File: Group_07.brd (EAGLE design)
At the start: 62.2 x 74.9 mm, 29 parts, among them J1 POWER_JACKPTH_LOCK, U1 +12v, U3 TCA9546ASO16, U4 TMUX1208

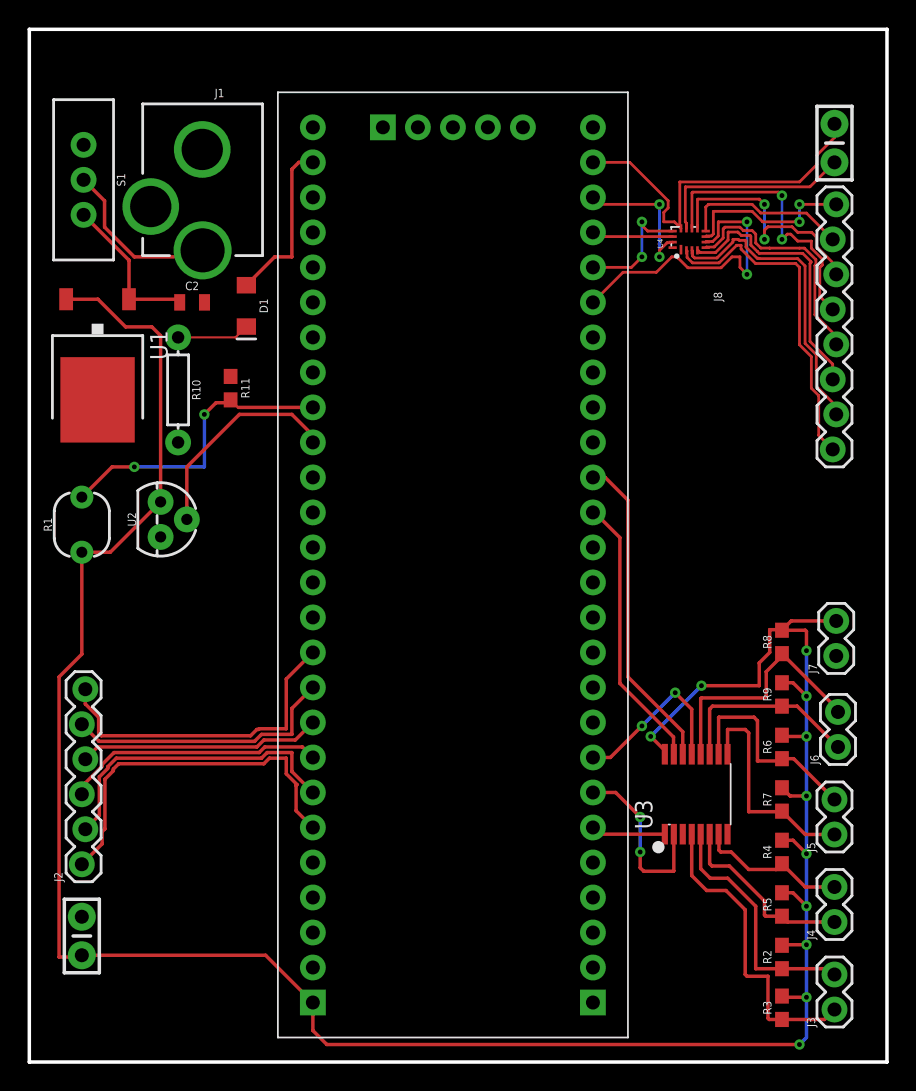
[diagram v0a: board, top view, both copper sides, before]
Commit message: controllo ratsnest
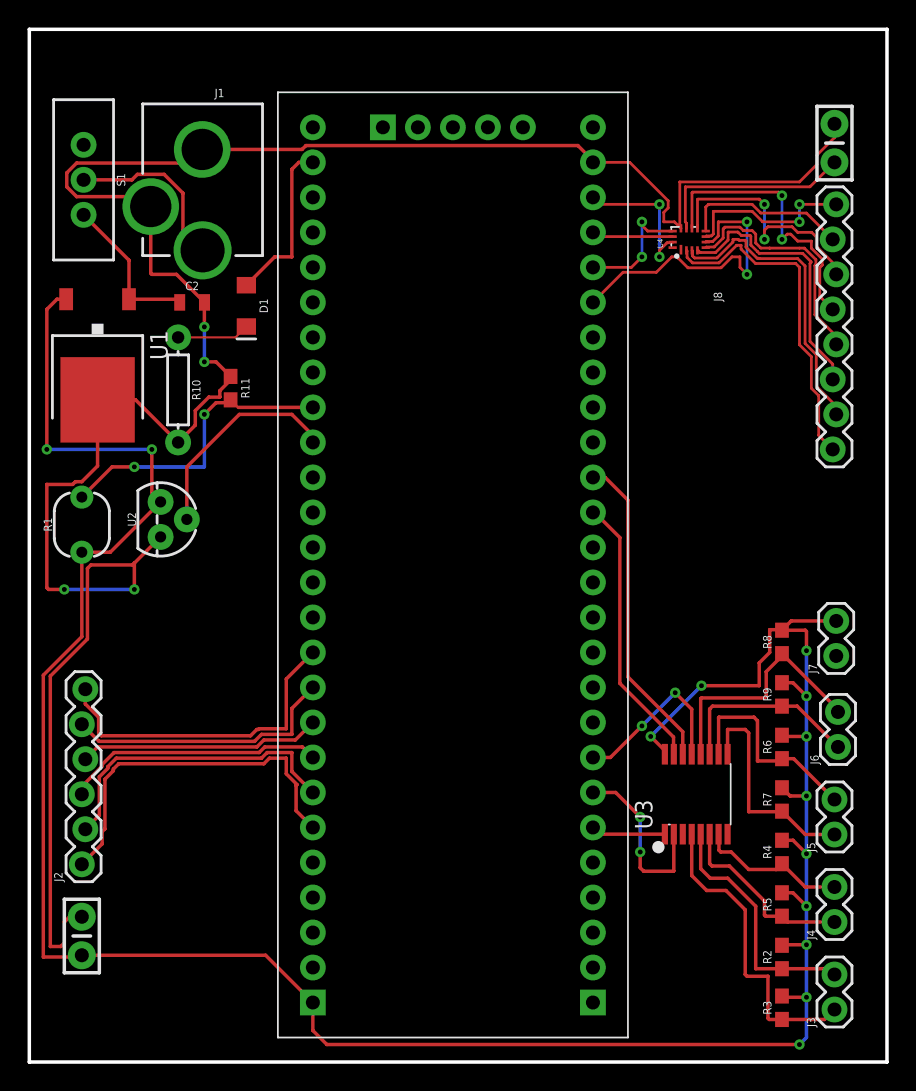
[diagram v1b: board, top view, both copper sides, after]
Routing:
- net GND: track 27.1 -> 168.3 mm, vias 0 -> 4
- net 5V: track 196.1 -> 201.3 mm, vias 11 -> 13
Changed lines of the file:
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@@
 <wire x1="56.642" y1="63.5" x2="58.42" y2="65.278" width="0.2032" layer="1"/>
 <wire x1="47.598" y1="63.5" x2="56.642" y2="63.5" width="0.2032" layer="1"/>
-<wire x1="2.673" y1="55.346" x2="4.979" y2="55.346" width="0.254" layer="1"/>
-<wire x1="6.985" y1="53.34" x2="8.89" y2="53.34" width="0.254" layer="1"/>
-<wire x1="8.89" y1="53.34" x2="9.525" y2="52.705" width="0.254" layer="1"/>
-<wire x1="9.525" y1="52.705" x2="9.525" y2="40.64" width="0.254" layer="1"/>
-<wire x1="4.979" y1="55.346" x2="6.985" y2="53.34" width="0.254" layer="1"/>
 <wire x1="9.525" y1="40.64" x2="5.874" y2="36.989" width="0.254" layer="1"/>
 <wire x1="5.874" y1="36.989" x2="3.81" y2="36.989" width="0.254" layer="1"/>
-<wire x1="3.81" y1="36.989" x2="3.81" y2="29.591" width="0.254" layer="1"/>
-<wire x1="3.81" y1="29.591" x2="2.159" y2="27.94" width="0.254" layer="1"/>
-<wire x1="2.159" y1="27.94" x2="2.159" y2="7.62" width="0.254" layer="1"/>
-<wire x1="2.159" y1="7.62" x2="3.683" y2="7.62" width="0.254" layer="1"/>
+<wire x1="3.81" y1="36.989" x2="3.81" y2="30.861" width="0.254" layer="1"/>
+<wire x1="3.81" y1="30.861" x2="1.016" y2="28.067" width="0.254" layer="1"/>
+<wire x1="1.016" y1="28.067" x2="1.016" y2="7.62" width="0.254" layer="1"/>
+<wire x1="1.016" y1="7.62" x2="3.683" y2="7.62" width="0.254" layer="1"/>
 <wire x1="3.683" y1="7.62" x2="3.81" y2="7.747" width="0.1524" layer="1"/>
 <wire x1="3.81" y1="7.747" x2="17.145" y2="7.747" width="0.254" layer="1"/>
@@
 <wire x1="20.574" y1="2.286" x2="20.574" y2="4.318" width="0.254" layer="1"/>
 <wire x1="55.88" y1="1.27" x2="21.59" y2="1.27" width="0.254" layer="1"/>
+<wire x1="9.525" y1="40.64" x2="8.89" y2="41.275" width="0.254" layer="1"/>
+<wire x1="8.89" y1="41.275" x2="8.89" y2="44.45" width="0.254" layer="1"/>
+<via x="8.89" y="44.45" extent="1-16" drill="0.35"/>
+<wire x1="8.89" y1="44.45" x2="1.27" y2="44.45" width="0.254" layer="16"/>
+<via x="1.27" y="44.45" extent="1-16" drill="0.35"/>
+<wire x1="1.27" y1="44.45" x2="1.27" y2="54.61" width="0.254" layer="1"/>
+<wire x1="1.27" y1="54.61" x2="2.006" y2="55.346" width="0.254" layer="1"/>
+<wire x1="2.006" y1="55.346" x2="2.673" y2="55.346" width="0.254" layer="1"/>
+<wire x1="54.61" y1="31.33" x2="47.679" y2="60.49" width="0" layer="19" extent="1-1"/>
 </signal>
 <signal name="N$1">
 <contactref element="J1" pad="PWR"/>
 <contactref element="S1" pad="2"/>
-<wire x1="3.937" y1="64.008" x2="5.461" y2="62.484" width="0.254" layer="1"/>
-<wire x1="7.62" y1="58.42" x2="12.0998" y2="58.42" width="0.254" layer="1"/>
-<wire x1="12.0998" y1="58.42" x2="12.573" y2="58.8932" width="0.254" layer="1"/>
-<wire x1="5.461" y1="62.484" x2="5.461" y2="60.579" width="0.254" layer="1"/>
-<wire x1="5.461" y1="60.579" x2="7.62" y2="58.42" width="0.254" layer="1"/>
+<wire x1="3.937" y1="64.008" x2="7.4436625" y2="64.008" width="0.254" layer="1"/>
+<wire x1="7.4436625" y1="64.008" x2="7.8434625" y2="64.4078" width="0.254" layer="1"/>
+<wire x1="7.8434625" y1="64.4078" x2="9.7793375" y2="64.4078" width="0.254" layer="1"/>
+<wire x1="9.7793375" y1="64.4078" x2="11.1482" y2="63.0389375" width="0.254" layer="1"/>
+<wire x1="11.1482" y1="60.318" x2="12.573" y2="58.8932" width="0.254" layer="1"/>
+<wire x1="11.1482" y1="63.0389375" x2="11.1482" y2="60.318" width="0.254" layer="1"/>
 </signal>
 <signal name="GND">
@@
 <wire x1="46.0344" y1="61.65033125" x2="46.3522" y2="61.96813125" width="0.2032" layer="1"/>
 <wire x1="46.3522" y1="62.49186875" x2="43.56606875" y2="65.278" width="0.2032" layer="1"/>
-<wire x1="43.56606875" y1="65.278" x2="40.894" y2="65.278" width="0.2032" layer="1"/>
+<wire x1="43.56606875" y1="65.278" x2="41.021" y2="65.278" width="0.2032" layer="1"/>
+<wire x1="41.021" y1="65.278" x2="40.894" y2="65.278" width="0.2032" layer="1"/>
 <wire x1="46.0344" y1="60.96" x2="46.809" y2="60.96" width="0.2032" layer="1"/>
 <wire x1="46.809" y1="60.96" x2="47.279" y2="60.49" width="0.2032" layer="1"/>
@@
 <wire x1="55.88" y1="63.8556" x2="57.15" y2="65.1256" width="0.2032" layer="1"/>
 <wire x1="57.15" y1="65.1256" x2="57.15" y2="65.80405625" width="0.2032" layer="1"/>
-<wire x1="58.42" y1="67.07405625" x2="58.42" y2="68.072" width="0.2032" layer="1"/>
-<wire x1="57.15" y1="65.80405625" x2="58.42" y2="67.07405625" width="0.2032" layer="1"/>
-<wire x1="50.662" y1="16.531" x2="47.412" y2="16.531" width="0" layer="19" extent="1-1"/>
-<wire x1="58.547" y1="29.464" x2="50.662" y2="16.531" width="0" layer="19" extent="1-1"/>
-<wire x1="9.525" y1="38.1" x2="10.795" y2="44.958" width="0" layer="19" extent="1-1"/>
-<wire x1="3.81" y1="10.541" x2="9.525" y2="38.1" width="0" layer="19" extent="1-1"/>
+<wire x1="58.42" y1="67.07405625" x2="57.15" y2="65.80405625" width="0.2032" layer="1"/>
+<wire x1="10.795" y1="44.958" x2="12.0424" y2="46.2054" width="0.254" layer="1"/>
+<wire x1="13.807" y1="48.2414" x2="13.8256" y2="48.26" width="0.254" layer="1"/>
+<wire x1="12.0424" y1="46.2054" x2="12.0424" y2="47.2623875" width="0.254" layer="1"/>
+<wire x1="12.0424" y1="47.2623875" x2="13.0214125" y2="48.2414" width="0.254" layer="1"/>
+<wire x1="13.0214125" y1="48.2414" x2="13.807" y2="48.2414" width="0.254" layer="1"/>
+<wire x1="13.8256" y1="48.26" x2="13.8256" y2="48.71073125" width="0.254" layer="1"/>
+<wire x1="14.605" y1="49.49013125" x2="14.605" y2="49.745" width="0.254" layer="1"/>
+<wire x1="13.8256" y1="48.71073125" x2="14.605" y2="49.49013125" width="0.254" layer="1"/>
+<wire x1="14.605" y1="49.745" x2="13.55" y2="50.8" width="0.254" layer="1"/>
+<wire x1="13.55" y1="50.8" x2="12.7" y2="50.8" width="0.254" layer="1"/>
+<via x="12.7" y="50.8" extent="1-16" drill="0.35"/>
+<wire x1="12.7" y1="50.8" x2="12.7" y2="53.34" width="0.254" layer="16"/>
+<via x="12.7" y="53.34" extent="1-16" drill="0.35"/>
+<wire x1="12.7" y1="53.34" x2="12.7" y2="55.107" width="0.254" layer="1"/>
+<wire x1="12.7" y1="55.107" x2="12.711" y2="55.118" width="0.254" layer="1"/>
+<wire x1="12.711" y1="55.118" x2="10.679" y2="57.15" width="0.254" layer="1"/>
+<wire x1="10.679" y1="57.15" x2="8.89" y2="57.15" width="0.254" layer="1"/>
+<wire x1="8.89" y1="57.15" x2="8.8114" y2="57.2286" width="0.254" layer="1"/>
+<wire x1="8.8114" y1="57.2286" x2="8.8114" y2="62.071" width="0.254" layer="1"/>
+<wire x1="3.4319875" y1="62.7888" x2="2.7178" y2="63.5029875" width="0.254" layer="1"/>
+<wire x1="2.7178" y1="63.5029875" x2="2.7178" y2="64.5130125" width="0.254" layer="1"/>
+<wire x1="2.7178" y1="64.5130125" x2="3.4319875" y2="65.2272" width="0.254" layer="1"/>
+<wire x1="8.8114" y1="62.071" x2="8.0936" y2="62.7888" width="0.254" layer="1"/>
+<wire x1="8.0936" y1="62.7888" x2="3.4319875" y2="62.7888" width="0.254" layer="1"/>
+<wire x1="11.5608" y1="65.2272" x2="12.5476" y2="66.214" width="0.254" layer="1"/>
+<wire x1="3.4319875" y1="65.2272" x2="11.5608" y2="65.2272" width="0.254" layer="1"/>
+<wire x1="12.5476" y1="66.214" x2="19.78833125" y2="66.214" width="0.254" layer="1"/>
+<wire x1="19.78833125" y1="66.214" x2="20.06973125" y2="66.4954" width="0.254" layer="1"/>
+<wire x1="20.06973125" y1="66.4954" x2="39.8036" y2="66.4954" width="0.254" layer="1"/>
+<wire x1="39.8036" y1="66.4954" x2="41.021" y2="65.278" width="0.254" layer="1"/>
+<wire x1="9.525" y1="38.1" x2="7.62" y2="36.195" width="0.254" layer="1"/>
+<wire x1="7.62" y1="36.195" x2="7.493" y2="36.068" width="0.254" layer="1"/>
+<wire x1="7.493" y1="36.068" x2="4.46953125" y2="36.068" width="0.254" layer="1"/>
+<wire x1="4.2164" y1="35.81486875" x2="4.2164" y2="30.6926625" width="0.254" layer="1"/>
+<wire x1="1.524" y1="28.0002625" x2="1.524" y2="8.382" width="0.254" layer="1"/>
+<wire x1="4.2164" y1="30.6926625" x2="1.524" y2="28.0002625" width="0.254" layer="1"/>
+<wire x1="1.524" y1="8.382" x2="2.286" y2="8.382" width="0.254" layer="1"/>
+<wire x1="2.286" y1="8.382" x2="2.54" y2="8.636" width="0.254" layer="1"/>
+<wire x1="2.54" y1="8.636" x2="2.54" y2="10.16" width="0.254" layer="1"/>
+<wire x1="2.54" y1="10.16" x2="2.921" y2="10.541" width="0.254" layer="1"/>
+<wire x1="2.921" y1="10.541" x2="3.81" y2="10.541" width="0.254" layer="1"/>
+<wire x1="4.46953125" y1="36.068" x2="4.2164" y2="35.81486875" width="0.254" layer="1"/>
+<wire x1="4.953" y1="48.046" x2="7.707" y2="48.046" width="0.254" layer="1"/>
+<wire x1="7.707" y1="48.046" x2="10.795" y2="44.958" width="0.254" layer="1"/>
+<wire x1="4.953" y1="48.046" x2="4.953" y2="43.2496" width="0.254" layer="1"/>
+<wire x1="4.953" y1="43.2496" x2="3.81" y2="42.1066" width="0.254" layer="1"/>
+<wire x1="3.81" y1="42.1066" x2="3.34706875" y2="42.1066" width="0.254" layer="1"/>
+<wire x1="3.34706875" y1="42.1066" x2="3.15046875" y2="41.91" width="0.254" layer="1"/>
+<wire x1="3.15046875" y1="41.91" x2="1.27" y2="41.91" width="0.254" layer="1"/>
+<wire x1="1.27" y1="41.91" x2="1.27" y2="34.417" width="0.254" layer="1"/>
+<wire x1="1.27" y1="34.417" x2="1.397" y2="34.29" width="0.254" layer="1"/>
+<wire x1="1.397" y1="34.29" x2="2.54" y2="34.29" width="0.254" layer="1"/>
+<via x="2.54" y="34.29" extent="1-16" drill="0.35"/>
+<wire x1="2.54" y1="34.29" x2="7.62" y2="34.29" width="0.254" layer="16"/>
+<via x="7.62" y="34.29" extent="1-16" drill="0.35"/>
+<wire x1="7.62" y1="34.29" x2="7.62" y2="36.195" width="0.254" layer="1"/>
+<wire x1="58.42" y1="68.072" x2="58.42" y2="67.07405625" width="0.254" layer="1"/>
+<wire x1="50.662" y1="16.531" x2="58.547" y2="29.464" width="0" layer="19" extent="1-1"/>
+<wire x1="47.412" y1="16.531" x2="50.662" y2="16.531" width="0" layer="19" extent="1-1"/>
+<wire x1="47.279" y1="60.49" x2="58.547" y2="29.464" width="0" layer="19" extent="1-1"/>
 </signal>
 <signal name="12V">

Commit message: aggiunta traces alimentazione e massa
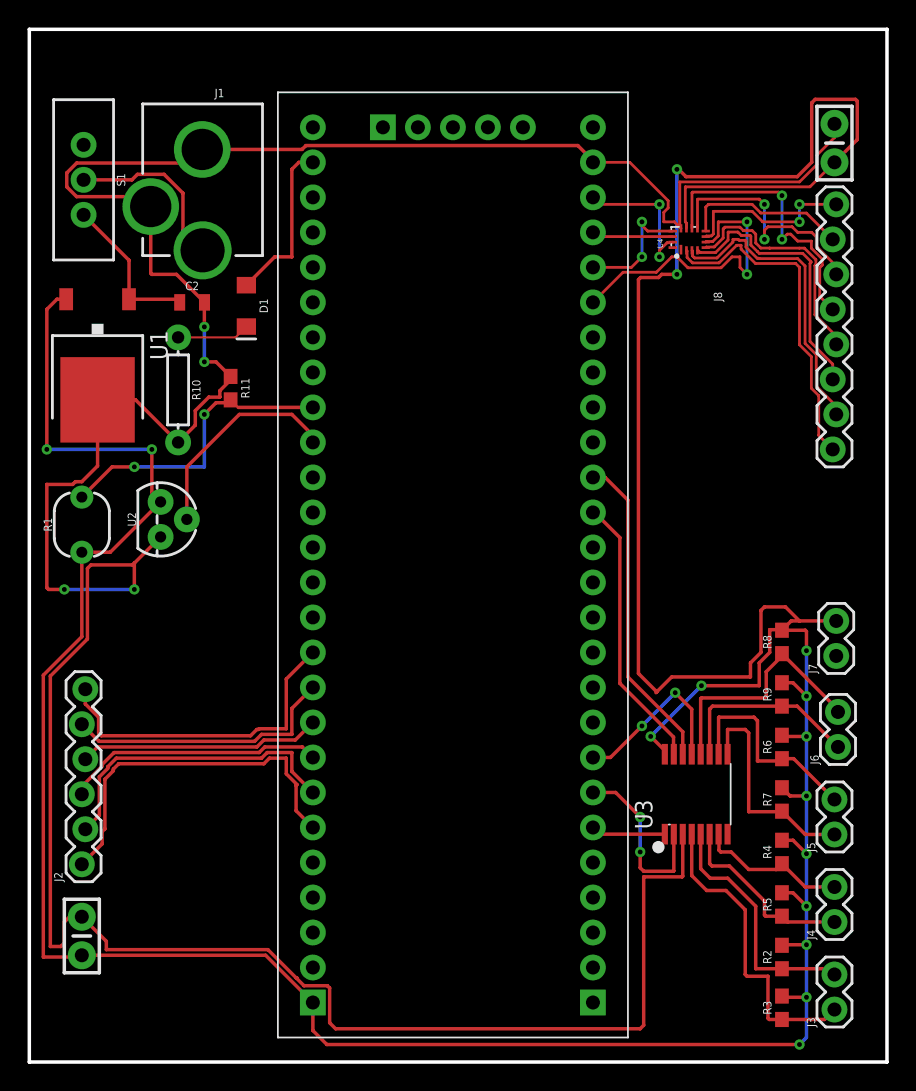
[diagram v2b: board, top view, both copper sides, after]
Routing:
- net 5V: track 201.3 -> 281.5 mm, vias 13 -> 15
- net GND: track 168.3 -> 231.1 mm
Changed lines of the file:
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@@
 </polygon>
 <wire x1="54.61" y1="31.33" x2="55.284" y2="32.004" width="0.254" layer="1"/>
-<wire x1="55.284" y1="32.004" x2="58.547" y2="32.004" width="0.254" layer="1"/>
+<wire x1="55.284" y1="32.004" x2="55.88" y2="32.004" width="0.254" layer="1"/>
+<wire x1="55.88" y1="32.004" x2="58.547" y2="32.004" width="0.254" layer="1"/>
 <wire x1="46.112" y1="22.331" x2="46.112" y2="22.595" width="0.254" layer="1"/>
 <wire x1="46.112" y1="22.595" x2="45.085" y2="23.622" width="0.254" layer="1"/>
@@
 <wire x1="1.27" y1="54.61" x2="2.006" y2="55.346" width="0.254" layer="1"/>
 <wire x1="2.006" y1="55.346" x2="2.673" y2="55.346" width="0.254" layer="1"/>
-<wire x1="54.61" y1="31.33" x2="47.679" y2="60.49" width="0" layer="19" extent="1-1"/>
+<wire x1="55.88" y1="32.004" x2="54.864" y2="33.02" width="0.254" layer="1"/>
+<wire x1="54.864" y1="33.02" x2="53.34" y2="33.02" width="0.254" layer="1"/>
+<wire x1="53.34" y1="33.02" x2="53.086" y2="32.766" width="0.254" layer="1"/>
+<wire x1="53.086" y1="32.766" x2="53.086" y2="29.718" width="0.254" layer="1"/>
+<wire x1="53.086" y1="29.718" x2="52.324" y2="28.956" width="0.254" layer="1"/>
+<wire x1="52.324" y1="28.956" x2="52.324" y2="27.94" width="0.254" layer="1"/>
+<wire x1="52.324" y1="27.94" x2="46.609" y2="27.94" width="0.254" layer="1"/>
+<wire x1="46.609" y1="27.94" x2="45.5295" y2="26.8605" width="0.254" layer="1"/>
+<wire x1="45.5295" y1="26.8605" x2="45.466" y2="26.797" width="0.254" layer="1"/>
+<wire x1="45.5295" y1="26.8605" x2="44.196" y2="28.194" width="0.254" layer="1"/>
+<wire x1="44.196" y1="56.769" x2="44.3484" y2="56.9214" width="0.254" layer="1"/>
+<wire x1="44.3484" y1="56.9214" x2="45.6542875" y2="56.9214" width="0.254" layer="1"/>
+<wire x1="45.8828875" y1="57.15" x2="46.99" y2="57.15" width="0.254" layer="1"/>
+<wire x1="45.6542875" y1="56.9214" x2="45.8828875" y2="57.15" width="0.254" layer="1"/>
+<via x="46.99" y="57.15" extent="1-16" drill="0.35"/>
+<wire x1="44.196" y1="28.194" x2="44.196" y2="56.769" width="0.254" layer="1"/>
+<wire x1="46.99" y1="57.15" x2="46.99" y2="64.77" width="0.254" layer="16"/>
+<via x="46.99" y="64.77" extent="1-16" drill="0.35"/>
+<wire x1="46.99" y1="64.77" x2="47.117" y2="64.77" width="0.254" layer="1"/>
+<wire x1="47.117" y1="64.77" x2="47.6504" y2="64.2366" width="0.254" layer="1"/>
+<wire x1="56.769" y1="65.28341875" x2="56.769" y2="69.596" width="0.254" layer="1"/>
+<wire x1="56.769" y1="69.596" x2="57.023" y2="69.85" width="0.254" layer="1"/>
+<wire x1="57.023" y1="69.85" x2="59.944" y2="69.85" width="0.254" layer="1"/>
+<wire x1="59.944" y1="69.85" x2="60.071" y2="69.723" width="0.254" layer="1"/>
+<wire x1="60.071" y1="66.929" x2="58.42" y2="65.278" width="0.254" layer="1"/>
+<wire x1="47.6504" y1="64.2366" x2="55.72218125" y2="64.2366" width="0.254" layer="1"/>
+<wire x1="55.72218125" y1="64.2366" x2="56.769" y2="65.28341875" width="0.254" layer="1"/>
+<wire x1="60.071" y1="69.723" x2="60.071" y2="66.929" width="0.254" layer="1"/>
 </signal>
 <signal name="N$1">
@@
 <wire x1="7.62" y1="34.29" x2="7.62" y2="36.195" width="0.254" layer="1"/>
 <wire x1="58.42" y1="68.072" x2="58.42" y2="67.07405625" width="0.254" layer="1"/>
-<wire x1="50.662" y1="16.531" x2="58.547" y2="29.464" width="0" layer="19" extent="1-1"/>
+<wire x1="3.81" y1="10.541" x2="5.588" y2="8.763" width="0.254" layer="1"/>
+<wire x1="5.588" y1="8.763" x2="5.588" y2="8.1534" width="0.254" layer="1"/>
+<wire x1="5.588" y1="8.1534" x2="17.3133375" y2="8.1534" width="0.254" layer="1"/>
+<wire x1="19.431" y1="6.096" x2="19.3707375" y2="6.096" width="0.254" layer="1"/>
+<wire x1="17.3133375" y1="8.1534" x2="19.3707375" y2="6.096" width="0.254" layer="1"/>
+<wire x1="19.3707375" y1="6.096" x2="19.9313375" y2="5.5354" width="0.254" layer="1"/>
+<wire x1="19.9313375" y1="5.5354" x2="21.62773125" y2="5.5354" width="0.254" layer="1"/>
+<wire x1="21.62773125" y1="5.5354" x2="21.7914" y2="5.37173125" width="0.254" layer="1"/>
+<wire x1="21.7914" y1="2.8466" x2="22.225" y2="2.413" width="0.254" layer="1"/>
+<wire x1="21.7914" y1="5.37173125" x2="21.7914" y2="2.8466" width="0.254" layer="1"/>
+<wire x1="22.225" y1="2.413" x2="44.323" y2="2.413" width="0.254" layer="1"/>
+<wire x1="44.577" y1="2.667" x2="44.577" y2="13.4366" width="0.254" layer="1"/>
+<wire x1="44.577" y1="13.4366" x2="47.371" y2="13.4366" width="0.254" layer="1"/>
+<wire x1="47.371" y1="13.4366" x2="47.412" y2="13.4776" width="0.254" layer="1"/>
+<wire x1="47.412" y1="13.4776" x2="47.412" y2="16.531" width="0.254" layer="1"/>
+<wire x1="44.323" y1="2.413" x2="44.577" y2="2.667" width="0.254" layer="1"/>
 <wire x1="47.412" y1="16.531" x2="50.662" y2="16.531" width="0" layer="19" extent="1-1"/>
-<wire x1="47.279" y1="60.49" x2="58.547" y2="29.464" width="0" layer="19" extent="1-1"/>
 </signal>
 <signal name="12V">
